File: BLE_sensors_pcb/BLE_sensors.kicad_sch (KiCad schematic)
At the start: 6 parts, among them J1 Conn_ARM_SWD_TagConnect_TC203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, J2 Conn_01x02, U4 ME54BS01

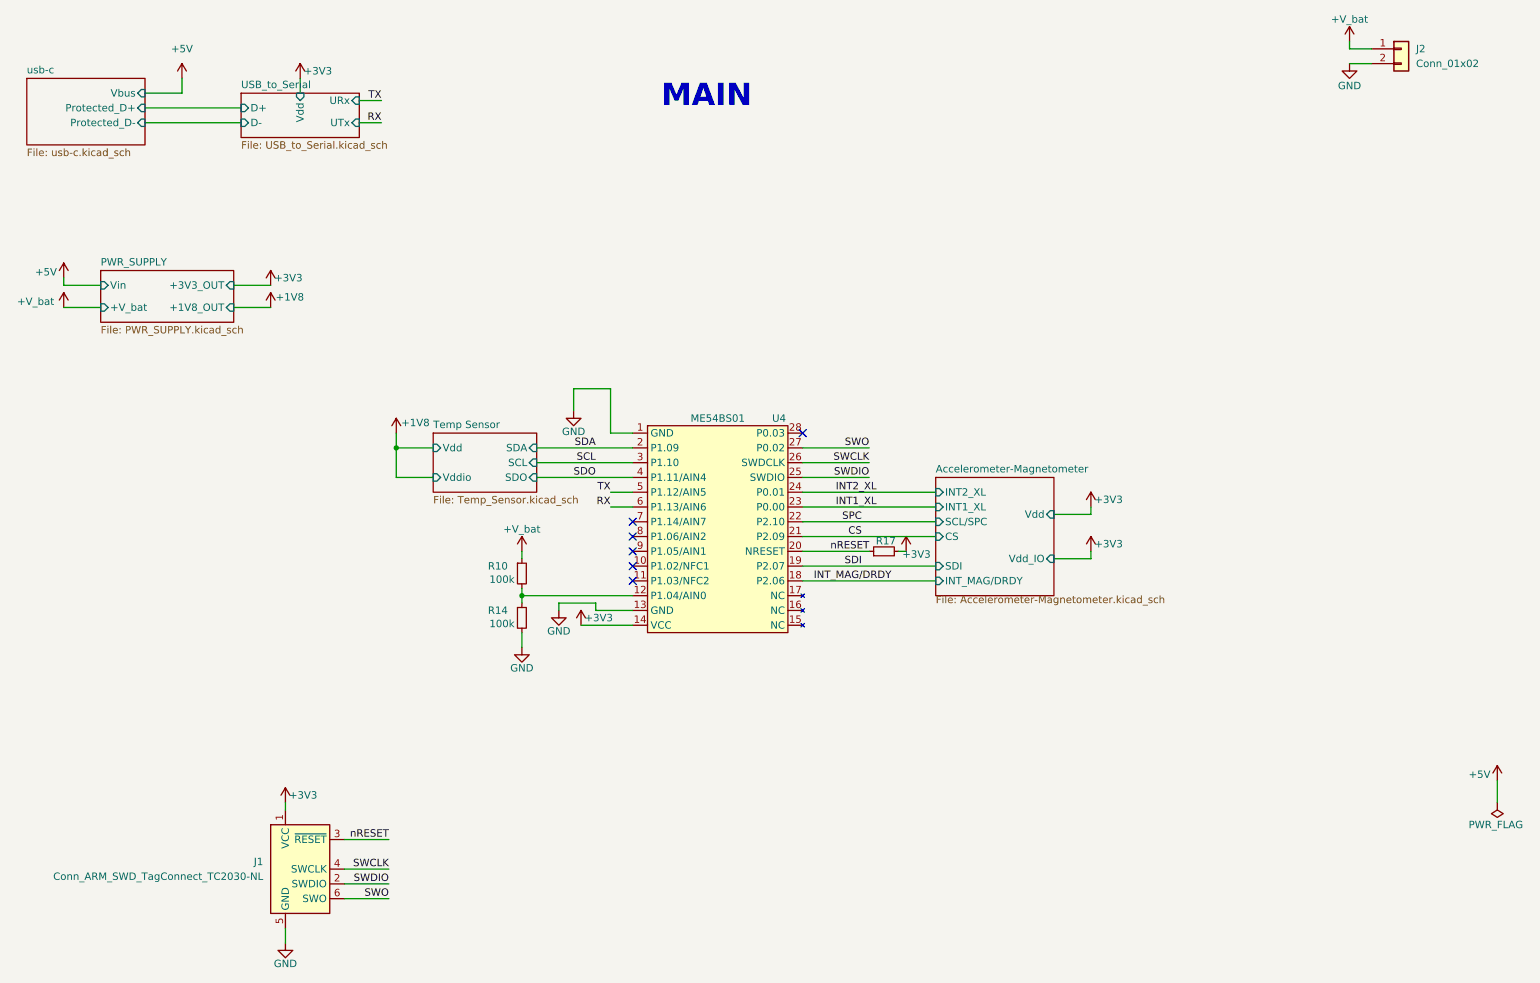
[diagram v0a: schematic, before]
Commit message: Changed bme power supply and added pull up to tag connect
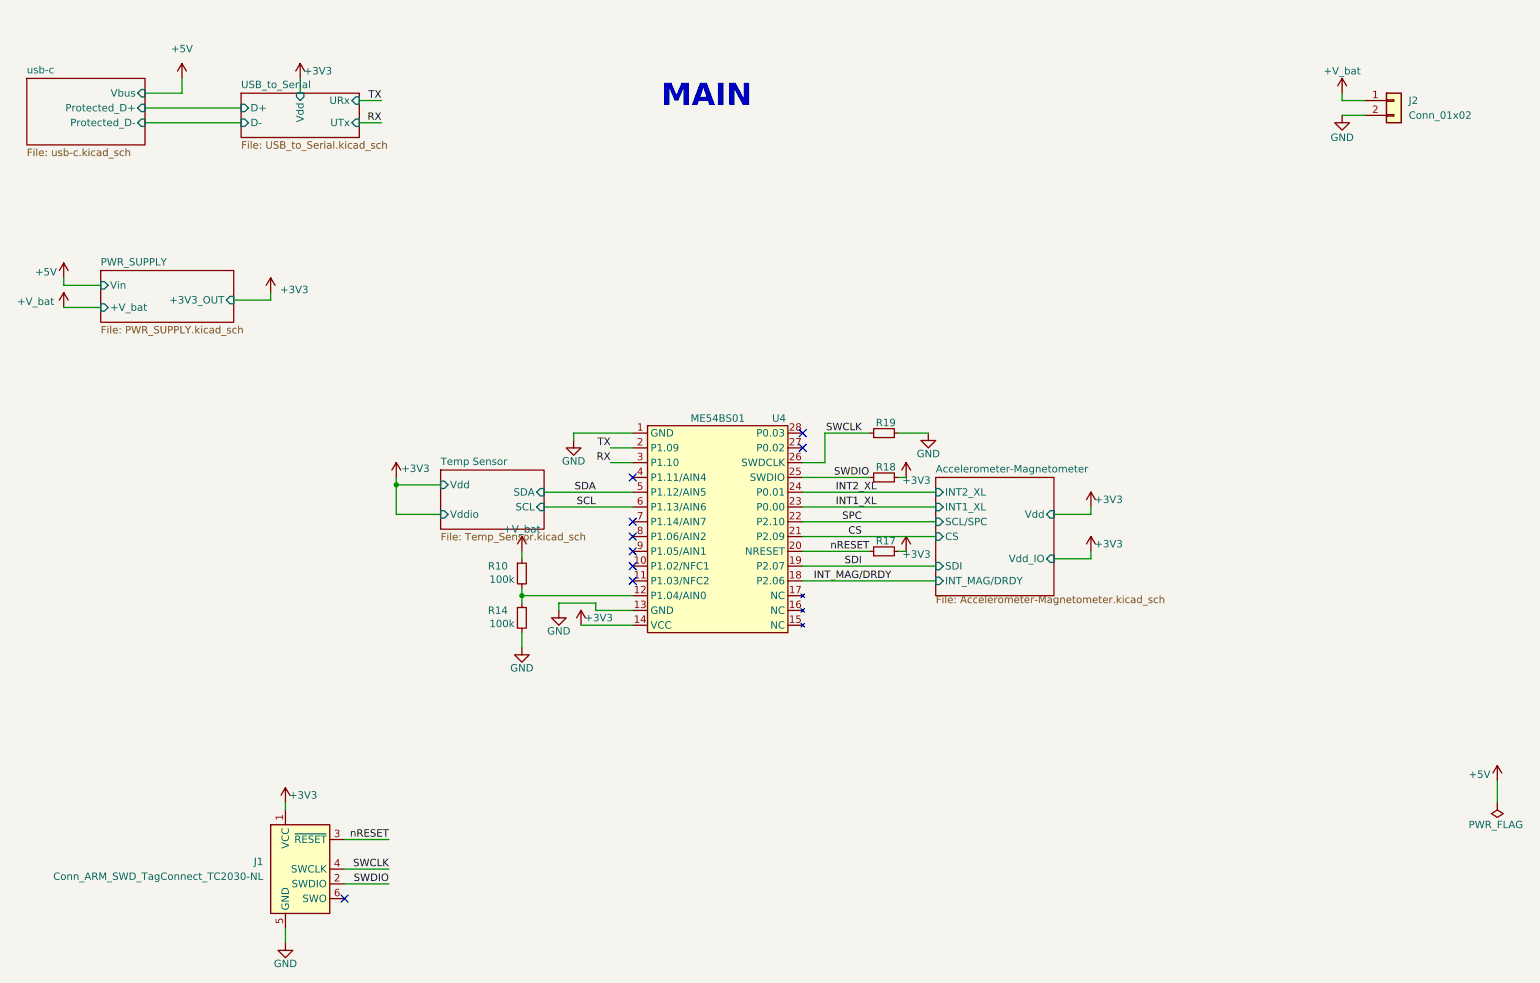
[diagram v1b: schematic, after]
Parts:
- added R18, R19: 10k, Resistor_SMD:R_0603_1608Metric, symbol Device:R_Small
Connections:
- net +3V3: now also R18.2
- net GND: now also R19.2
- net RX: now also U4.3 (P1.10); no longer U4.6 (P1.13/AIN6)
- net SCL: now also U4.6 (P1.13/AIN6); no longer U4.3 (P1.10)
- net SDA: now also U4.5 (P1.12/AIN5); no longer U4.2 (P1.09)
- net SWCLK: now also R19.1
- net SWDIO: now also R18.1
- net TX: now also U4.2 (P1.09); no longer U4.5 (P1.12/AIN5)
- net SDO: no longer names the net of U4.4 (P1.11/AIN4)
- net SWO: no longer names the net of U4.27 (P0.02)
- net SWO: no longer J1.6 (SWO)
- no-connect marks 6 -> 9
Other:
- sheet PWR_SUPPLY ports: added none; removed +1V8_OUT
- sheet Temp Sensor ports: added none; removed SDO
- moved on the sheet: J2
